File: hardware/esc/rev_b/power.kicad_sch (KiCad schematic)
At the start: 35 parts, among them J701 AUX_BATTERY, J702 FLIGHT_CAN_POWER, U701 LM5164DDA, U702 AP2112K-3.3TRG1, U703 LM5164DDA

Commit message: build: generate rev-b outputs
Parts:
- C700, C701, C702, C703, C704, C705, C706, C707, C708, C709, C710, C711, C712, C713, C714, C715, C716, D701, F701, J701, J702, L701, L702, R701, R702, R703, R704, R705, R710, R711, R712, R713, U701, U702, U703: hierarchy_path /98734485-5dd9-43e3-8e43-27cf828371fb/ec6b5b42-0504-447b-87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 -> /94616530-9a4d-4eb4-ab8e-589eb49d9ab4/15ca008e-0b7b-45bb-93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

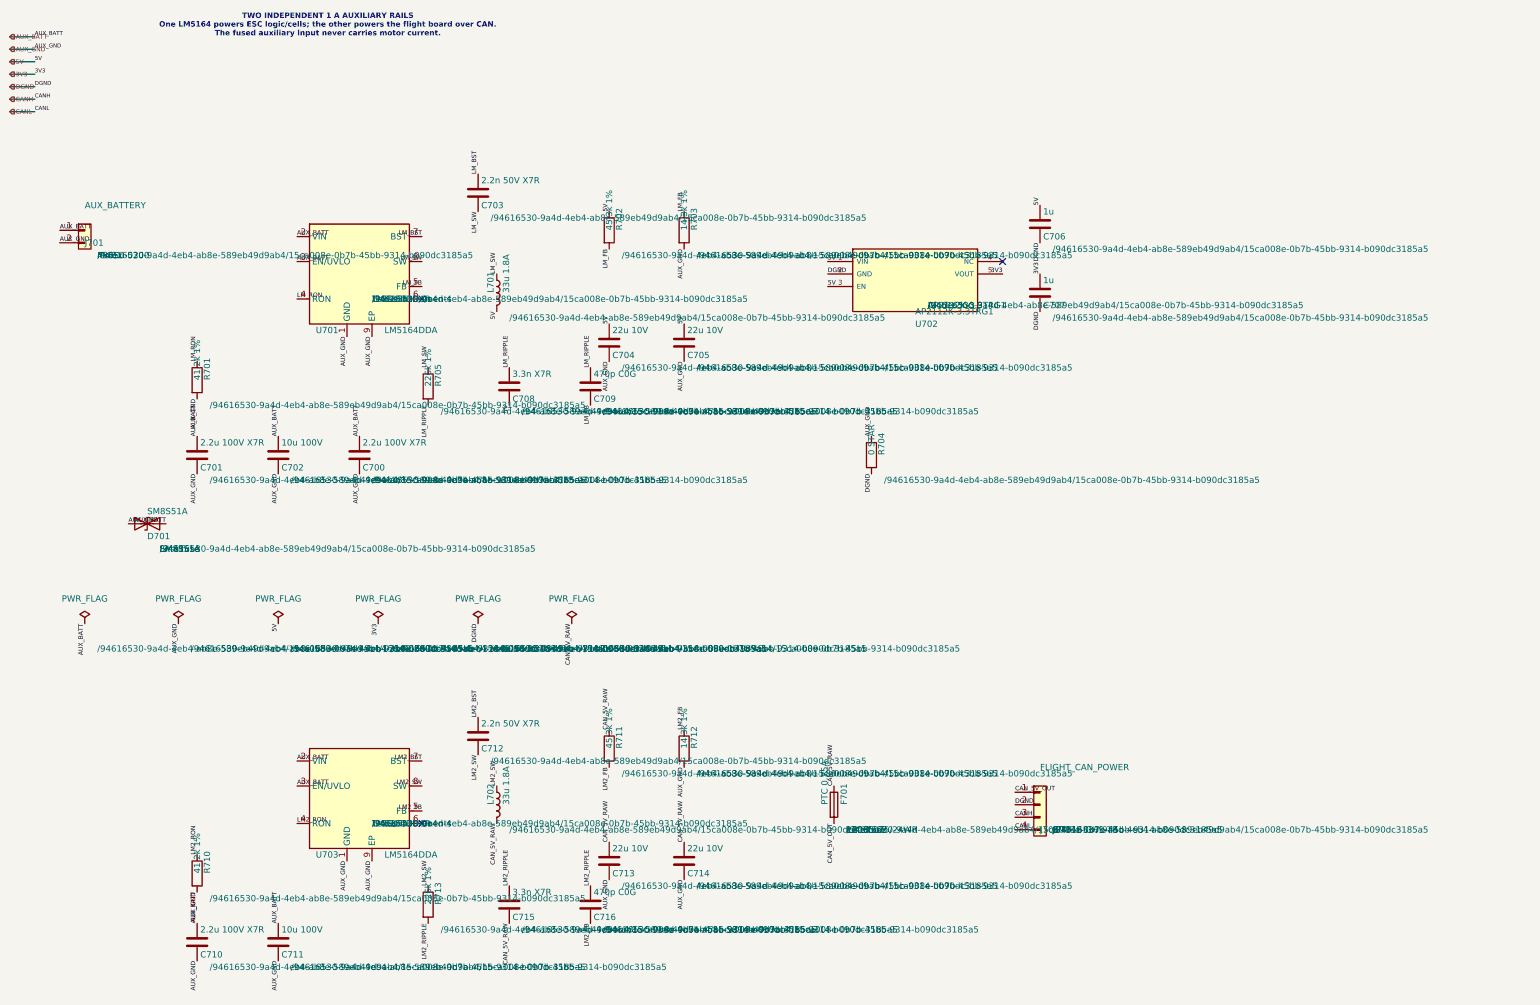
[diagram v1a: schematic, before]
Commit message: build: route and validate rev-b boards
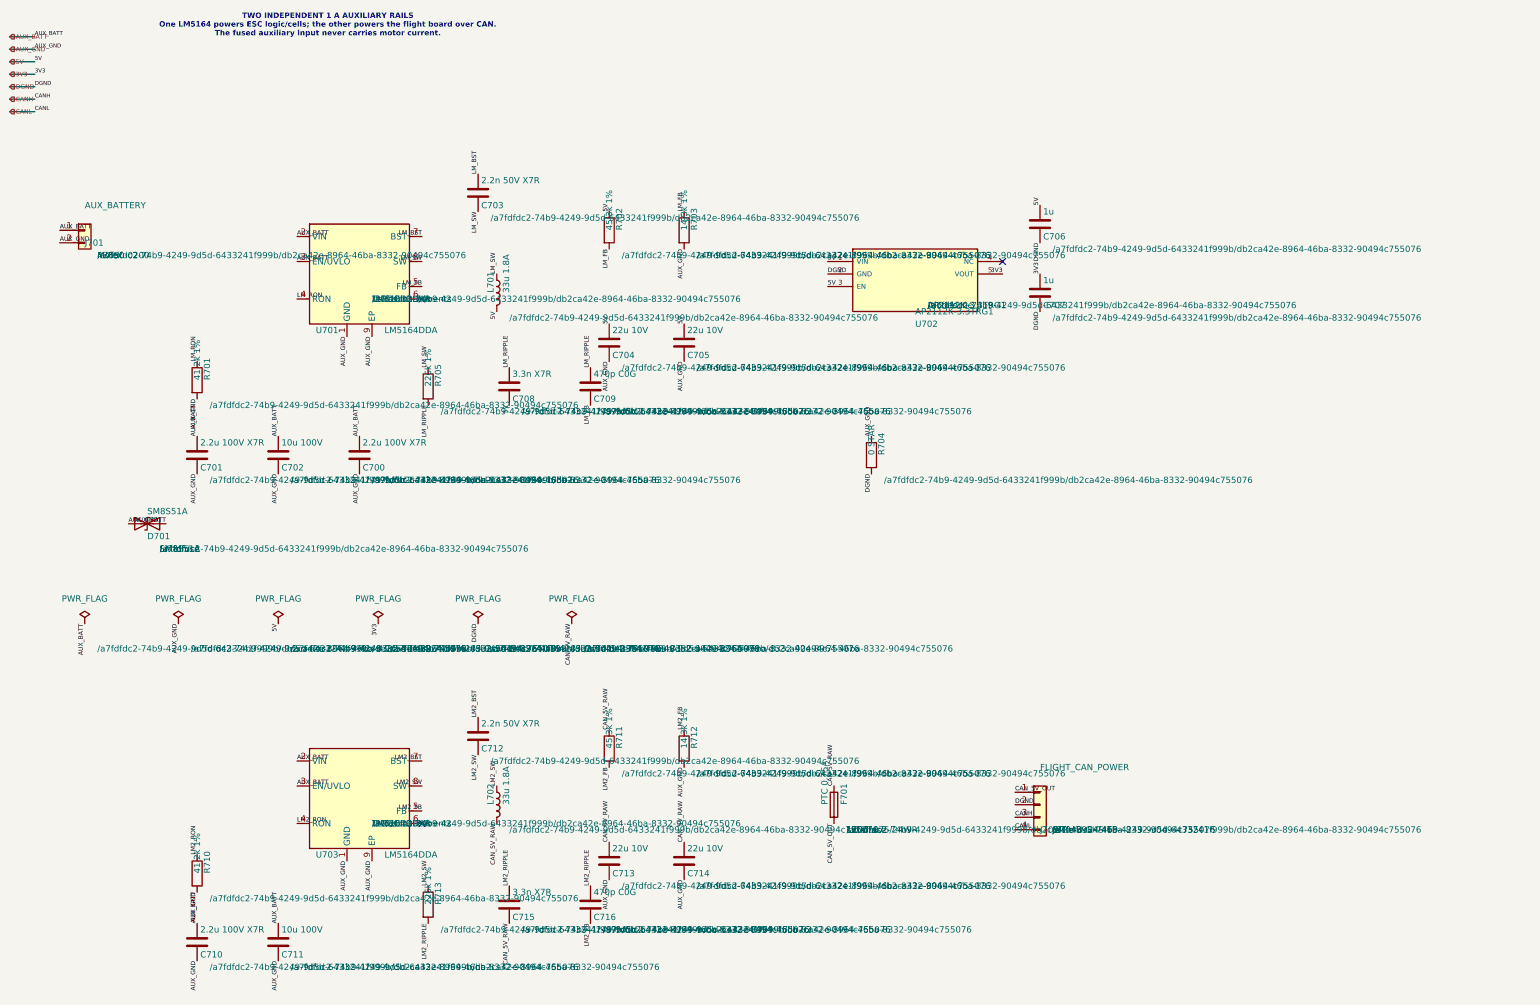
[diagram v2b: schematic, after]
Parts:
- C700, C701, C702, C703, C704, C705, C706, C707, C708, C709, C710, C711, C712, C713, C714, C715, C716, D701, F701, J701, J702, L701, L702, R701, R702, R703, R704, R705, R710, R711, R712, R713, U701, U702, U703: hierarchy_path /94616530-9a4d-4eb4-ab8e-589eb49d9ab4/15ca008e-0b7b-45bb-93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 -> /a7fdfdc2-74b9-4249-9d5d-6433241f999b/db2ca42e-8964-46ba-83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

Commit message: build: route and validate rev-b boards
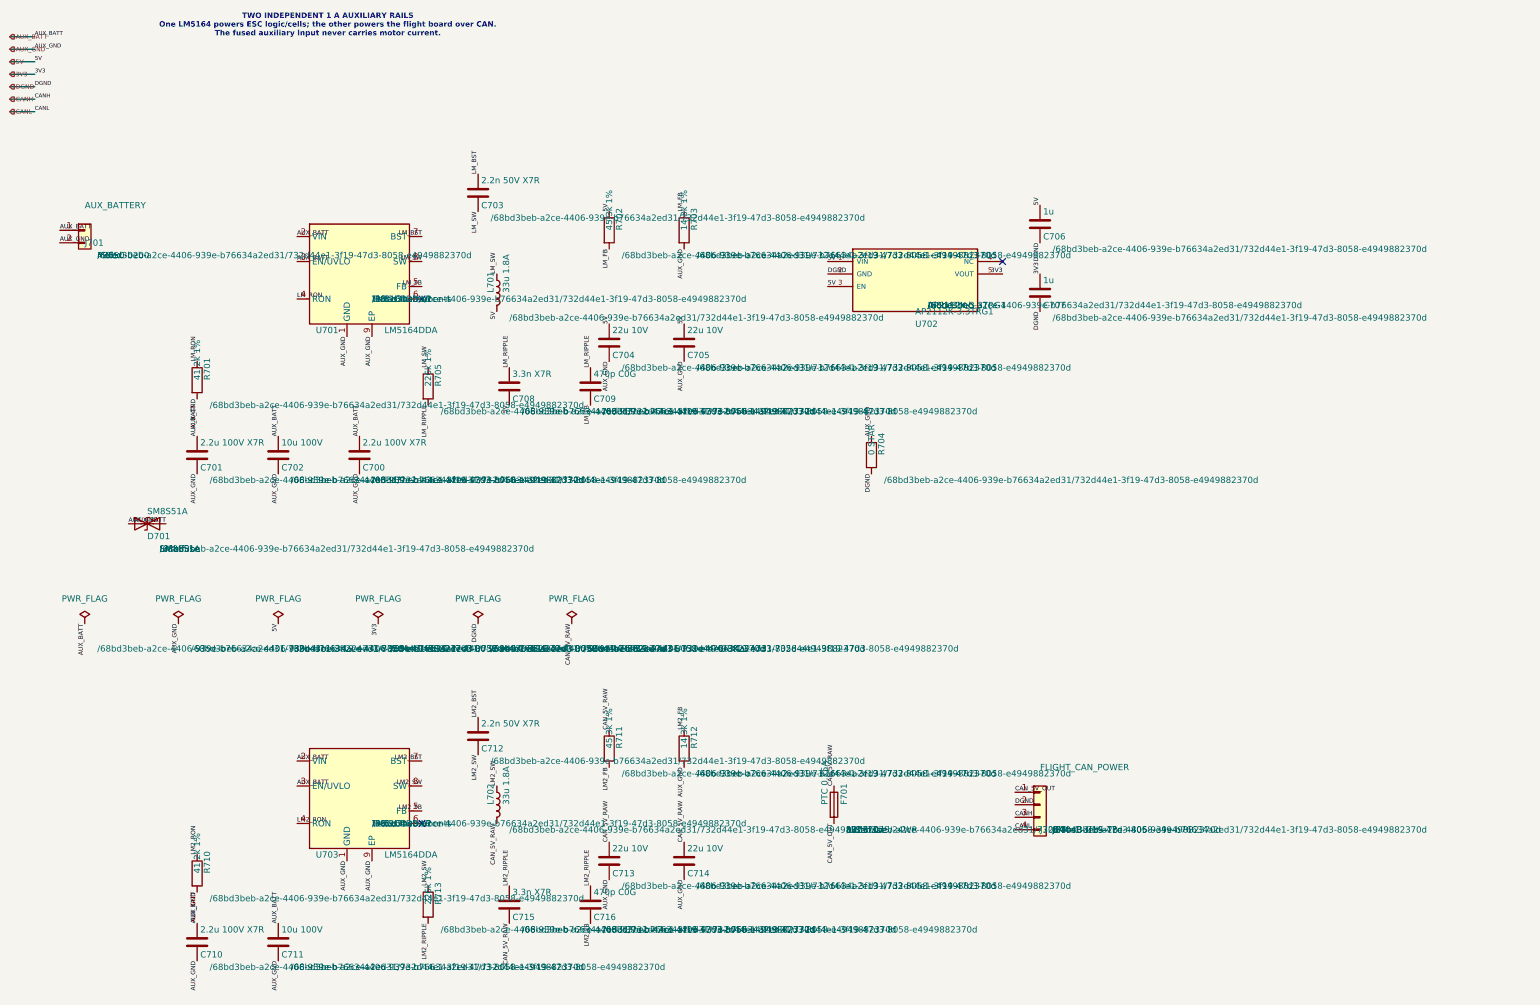
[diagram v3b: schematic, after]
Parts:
- C700, C701, C702, C703, C704, C705, C706, C707, C708, C709, C710, C711, C712, C713, C714, C715, C716, D701, F701, J701, J702, L701, L702, R701, R702, R703, R704, R705, R710, R711, R712, R713, U701, U702, U703: hierarchy_path /a7fdfdc2-74b9-4249-9d5d-6433241f999b/db2ca42e-8964-46ba-83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 -> /68bd3beb-a2ce-4406-939e-b76634a2ed31/732d44e1-3f19-47d3-80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

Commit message: build: route and validate rev-b boards
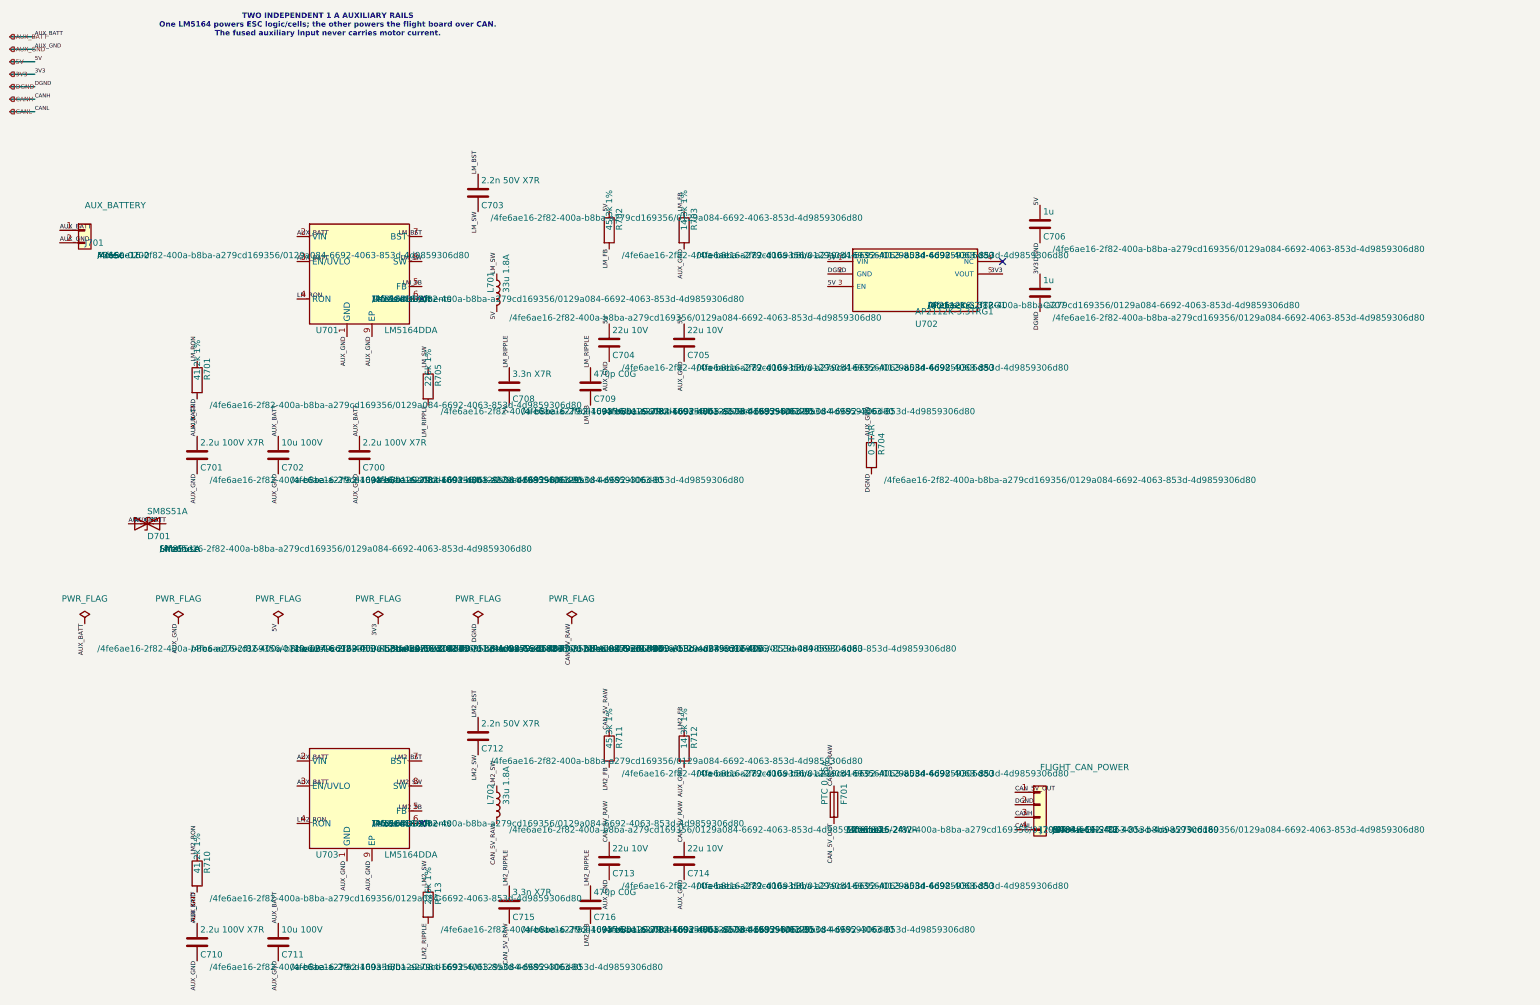
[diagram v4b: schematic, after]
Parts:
- C700, C701, C702, C703, C704, C705, C706, C707, C708, C709, C710, C711, C712, C713, C714, C715, C716, D701, F701, J701, J702, L701, L702, R701, R702, R703, R704, R705, R710, R711, R712, R713, U701, U702, U703: hierarchy_path /68bd3beb-a2ce-4406-939e-b76634a2ed31/732d44e1-3f19-47d3-80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 -> /4fe6ae16-2f82-400a-b8ba-a279cd169356/0129a084-6692-4063-85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
